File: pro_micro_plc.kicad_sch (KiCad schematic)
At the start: 35 parts, among them J1 Conn_01x06_Pin, J2 Conn_01x02_Socket, J3 Conn_01x02_Socket, J4 Conn_01x02_Socket, J5 Conn_01x02_Pin, J6 Conn_01x04_Pin, Q1 2N7002K, Q2 2N7002K, Q3 2N7002K, Q4 2N7002K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

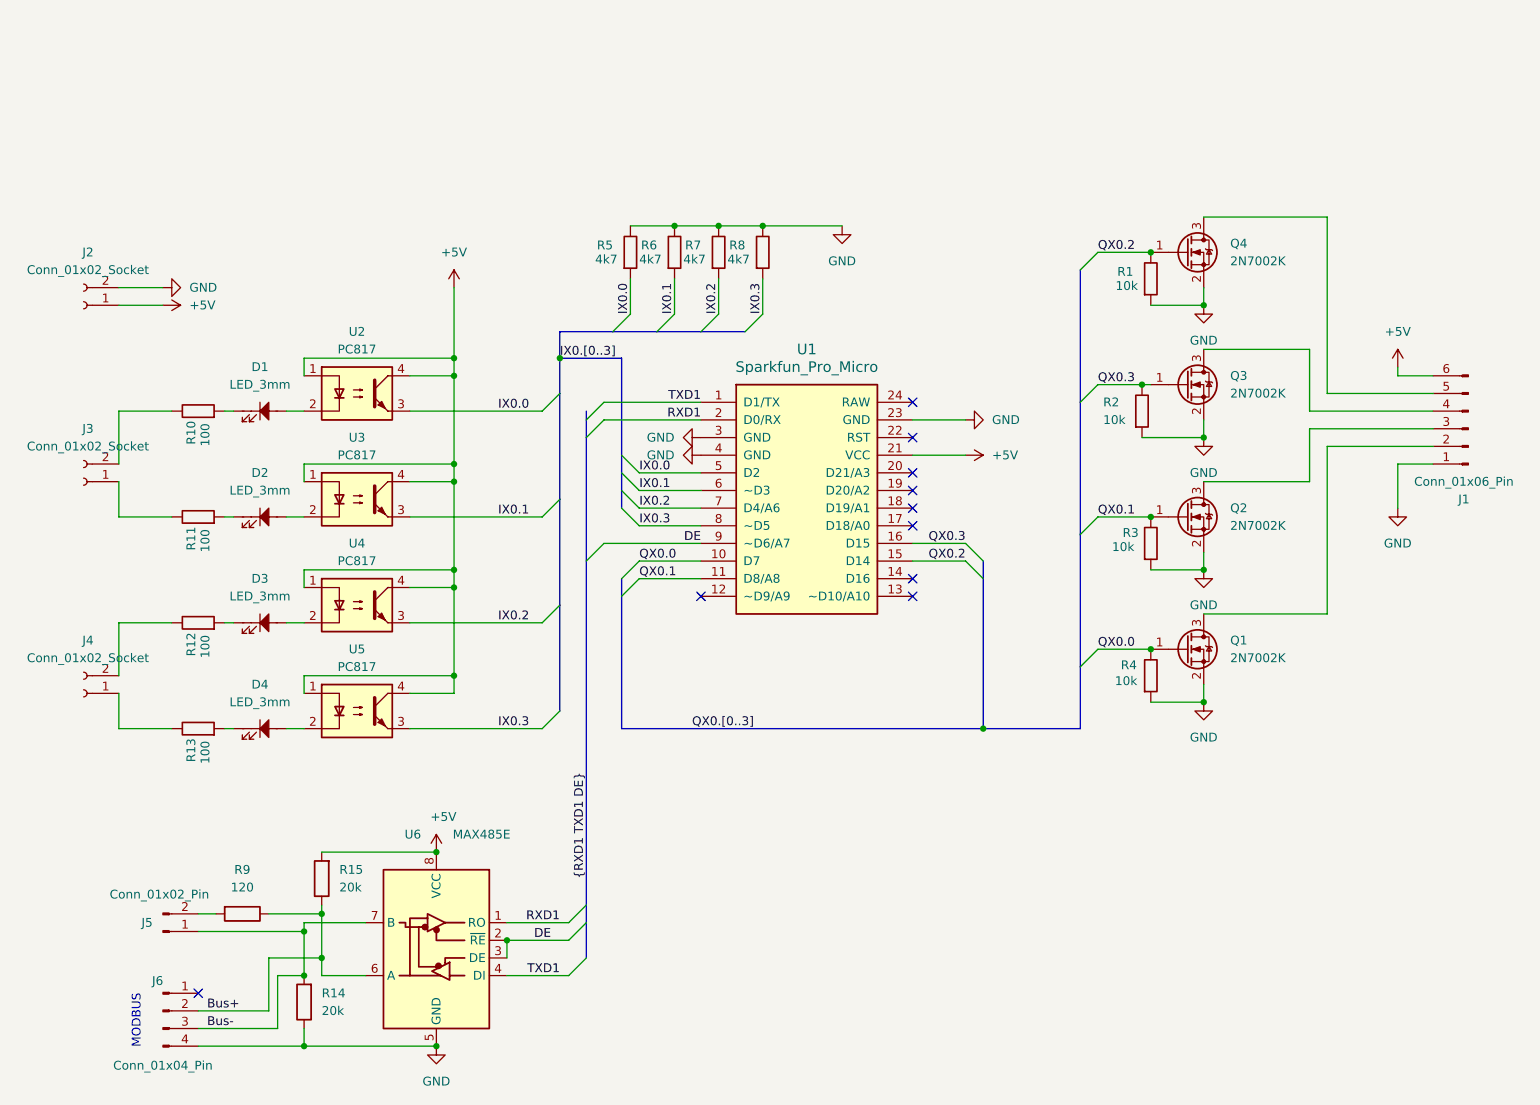
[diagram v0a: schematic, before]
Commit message: add analog input
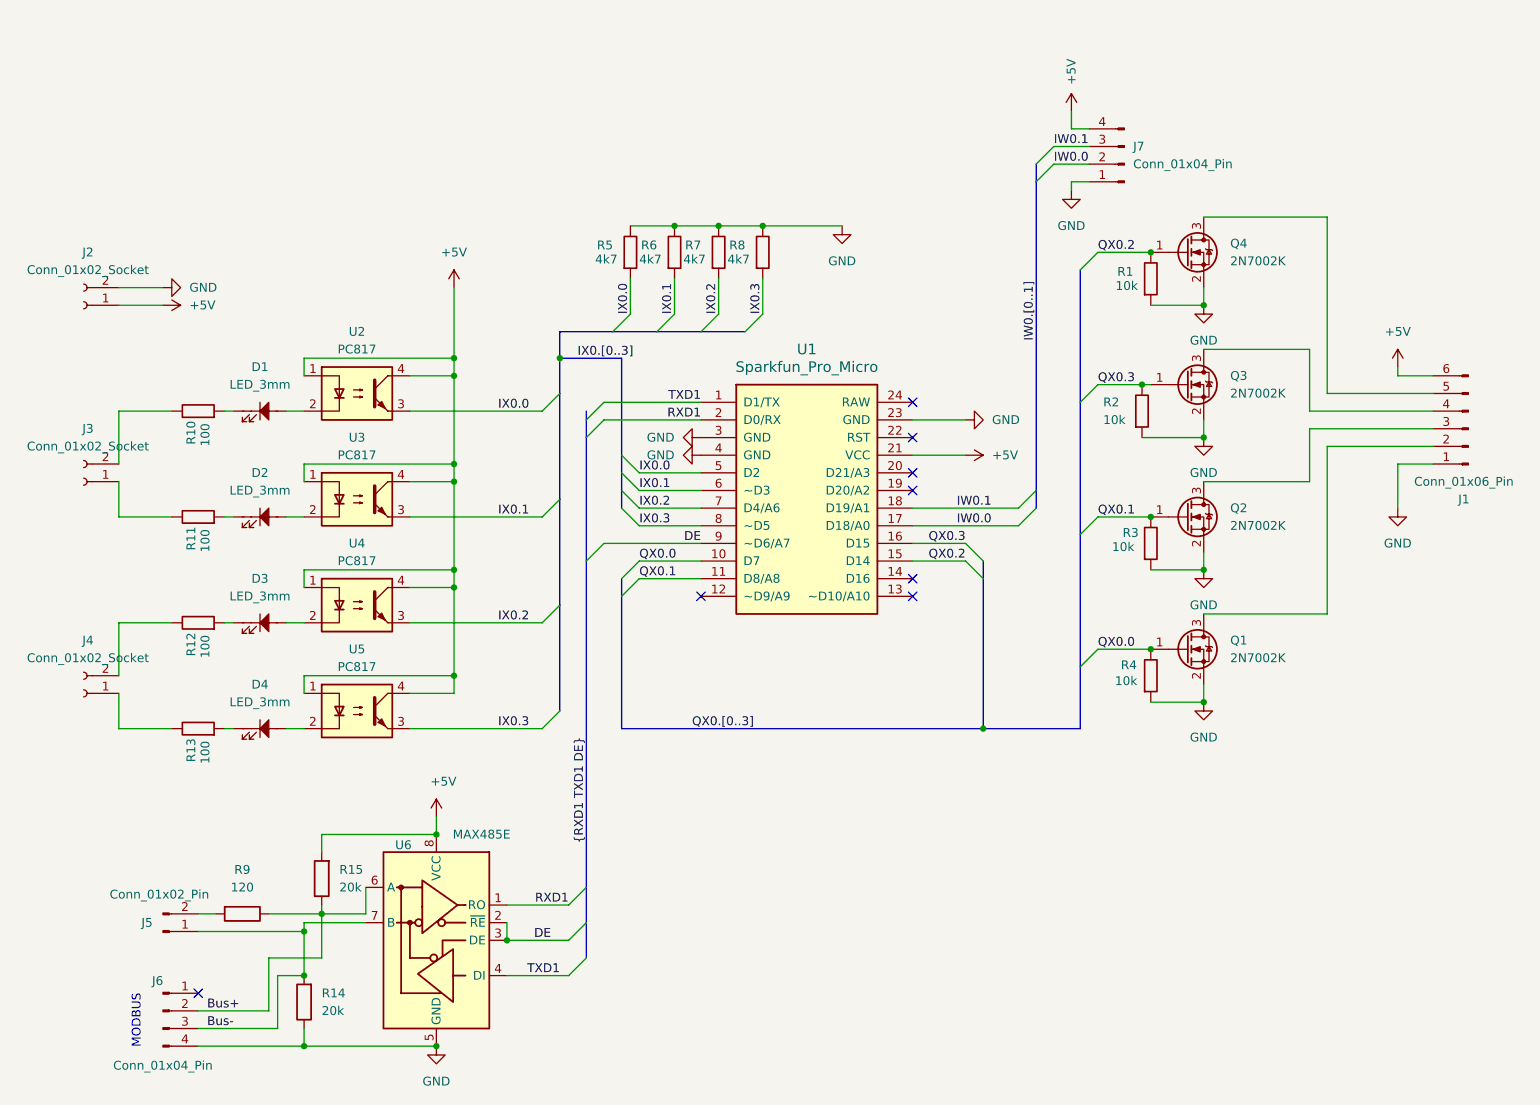
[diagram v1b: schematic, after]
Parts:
- added J7: Conn_01x04_Pin, Connector_PinHeader_2.54mm:PinHeader_1x04_P2.54mm_Vertical, symbol Connector:Conn_01x04_Pin
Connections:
- net +5V: now also J7.4 (Pin_4)
- net GND: now also J7.1 (Pin_1)
- net IW0.0: now reaches U1.17 (D18/A0)
- net IW0.0: now also J7.2 (Pin_2)
- net IW0.1: now reaches U1.18 (D19/A1)
- net IW0.1: now also J7.3 (Pin_3)
- no-connect marks 10 -> 8

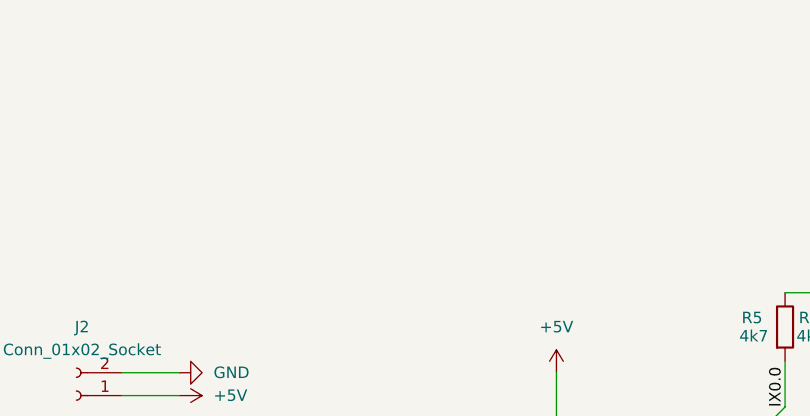
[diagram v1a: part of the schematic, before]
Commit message: more space for max485 and vias on ground
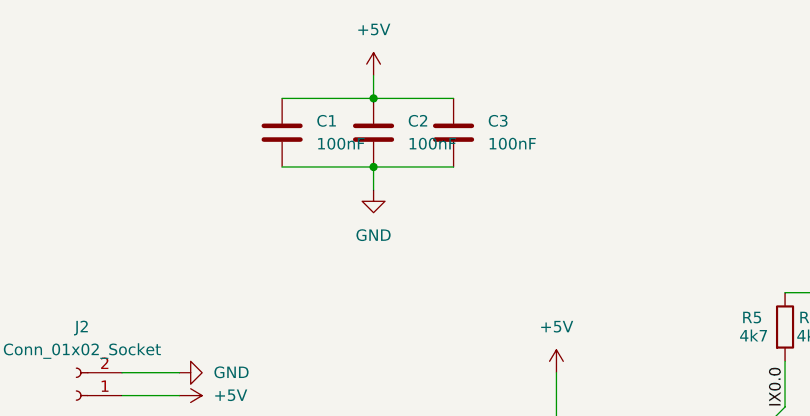
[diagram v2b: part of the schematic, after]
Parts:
- added C1, C2, C3: 100nF, Capacitor_SMD:C_0805_2012Metric_Pad1.18x1.45mm_HandSolder, symbol Device:C
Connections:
- net +5V: now also C1.1, C2.1, C3.1
- net GND: now also C1.2, C2.2, C3.2

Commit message: update terminal blocks
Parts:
- J2, J3, J4: footprint TerminalBlock_Phoenix:TerminalBlock_Phoenix_MKDS-1,5-2-5.08_1x02_P5.08mm_Horizontal -> TerminalBlock_Phoenix:TerminalBlock_Phoenix_MKDS-1,5-2_1x02_P5.00mm_Horizontal
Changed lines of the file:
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@@
 			)
 		)
-		(property "Footprint" "TerminalBlock_Phoenix:TerminalBlock_Phoenix_MKDS-1,5-2-5.08_1x02_P5.08mm_Horizontal"
+		(property "Footprint" "TerminalBlock_Phoenix:TerminalBlock_Phoenix_MKDS-1,5-2_1x02_P5.00mm_Horizontal"
 			(at 31.75 64.77 0)
 			(effects
@@
 			)
 		)
-		(property "Footprint" "TerminalBlock_Phoenix:TerminalBlock_Phoenix_MKDS-1,5-2-5.08_1x02_P5.08mm_Horizontal"
+		(property "Footprint" "TerminalBlock_Phoenix:TerminalBlock_Phoenix_MKDS-1,5-2_1x02_P5.00mm_Horizontal"
 			(at 31.75 120.65 0)
 			(effects
@@
 			)
 		)
-		(property "Footprint" "TerminalBlock_Phoenix:TerminalBlock_Phoenix_MKDS-1,5-2-5.08_1x02_P5.08mm_Horizontal"
+		(property "Footprint" "TerminalBlock_Phoenix:TerminalBlock_Phoenix_MKDS-1,5-2_1x02_P5.00mm_Horizontal"
 			(at 31.75 90.17 0)
 			(effects

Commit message: Update README
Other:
- company: (none) -> JbLb
- title: (none) -> Micro pro PLC
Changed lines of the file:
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@@
 	(generator_version "8.0")
 	(paper "A4")
+	(title_block
+		(title "Micro pro PLC")
+		(date "2024-09-08")
+		(rev "1.0")
+		(company "JbLb")
+	)
+	(bus_alias ""
+		(members)
+	)
 	(junction
 		(at 85.09 105.41)
